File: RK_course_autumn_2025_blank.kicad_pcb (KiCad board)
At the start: 2 copper layers, 65 x 80 mm, 24 parts, among them J1 JST-ZH 6pin, J2 JST-ZH 6pin, J3 Conn_01x02, J4 JST-ZH 6pin, J5 JST-ZH 6pin, J6 Conn_01x03

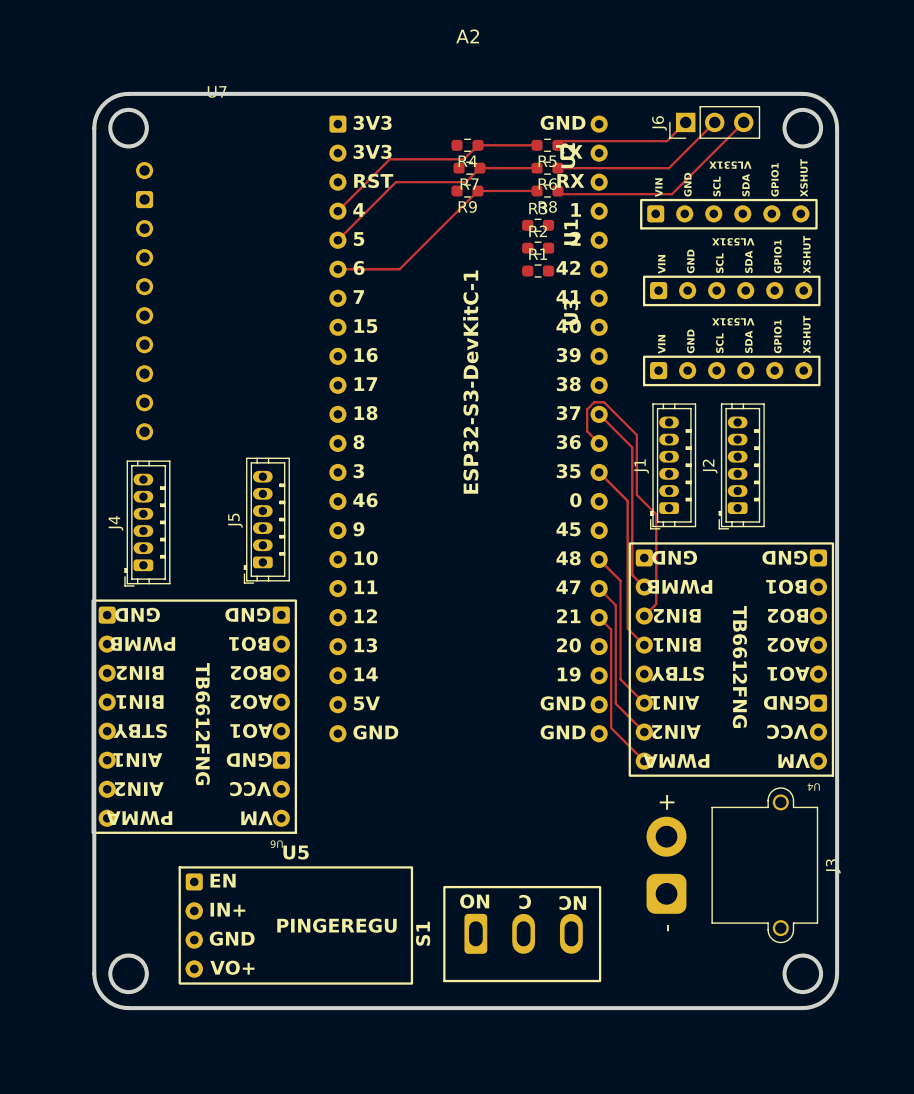
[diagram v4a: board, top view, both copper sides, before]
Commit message: Added traces to PCB to see if possible. Has to be done again.
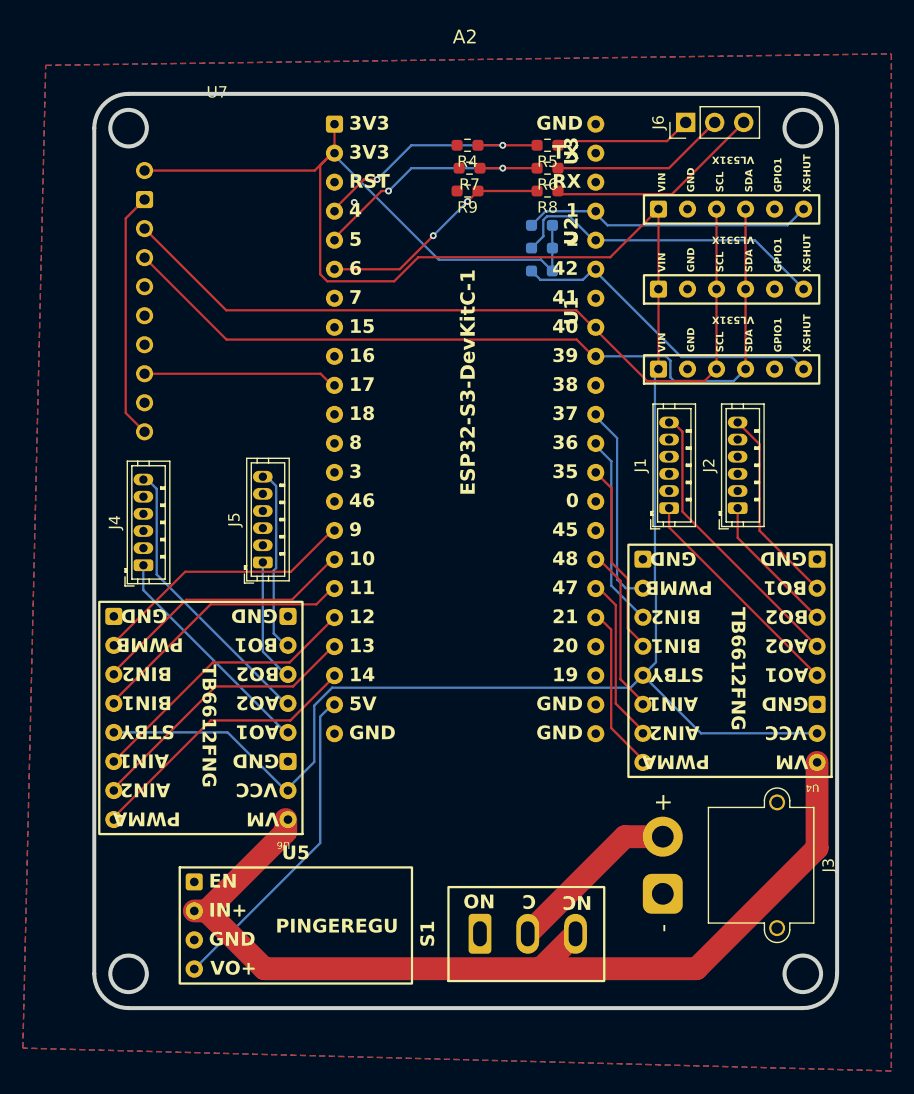
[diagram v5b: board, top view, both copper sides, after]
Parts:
- R1, R2, R3: moved to B.Cu
- moved U3 14.1 mm to (78.0, 70.5)
- moved U1 6.87 mm to (78.0, 84.5)
- moved U2 6.58 mm to (78.0, 77.5)
- moved U6 0.59 mm to (53.2, 129.0)
- moved S1 0.36 mm to (70.0, 139.0)
- moved R1 0.34 mm to (75.4, 81.0), turned to 180 degrees
- moved R2 0.34 mm to (75.4, 79.0), turned to 180 degrees
- moved R3 0.34 mm to (75.4, 77.0), turned to 180 degrees
- moved J3 0.33 mm to (86.0, 135.5)
- moved A2 0.30 mm to (68.7, 68.1)
- moved U4 0.16 mm to (99.5, 124.0)
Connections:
- U7 pad 1: +5V -> +3V3
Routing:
- net +3V3: track 0.00 -> 204.6 mm
- net +12V: track 0.00 -> 83.6 mm
- net SDA: track 0.00 -> 72.4 mm
- net SCL: track 0.00 -> 70.0 mm
- net XSHUT2: track 0.00 -> 28.4 mm
- net +5V: track 0.00 -> 28.1 mm
- net XSHUT1: track 0.00 -> 28.1 mm
- net XSHUT3: track 0.00 -> 25.4 mm
- net Net-(J1-Pin_6): track 0.00 -> 24.8 mm
- net Net-(J4-Pin_6): track 0.00 -> 24.6 mm
- net MOT3DIR2: track 0.00 -> 24.5 mm
- net MOT3DIR1: track 0.00 -> 24.5 mm
- net MOT3SPEED: track 0.00 -> 24.4 mm
- net MOT4SPEED: track 0.00 -> 23.5 mm
- net MOT4DIR1: track 0.00 -> 23.5 mm
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- added copper zone on B.Cu, net GND
- added copper zone on F.Cu, net GND

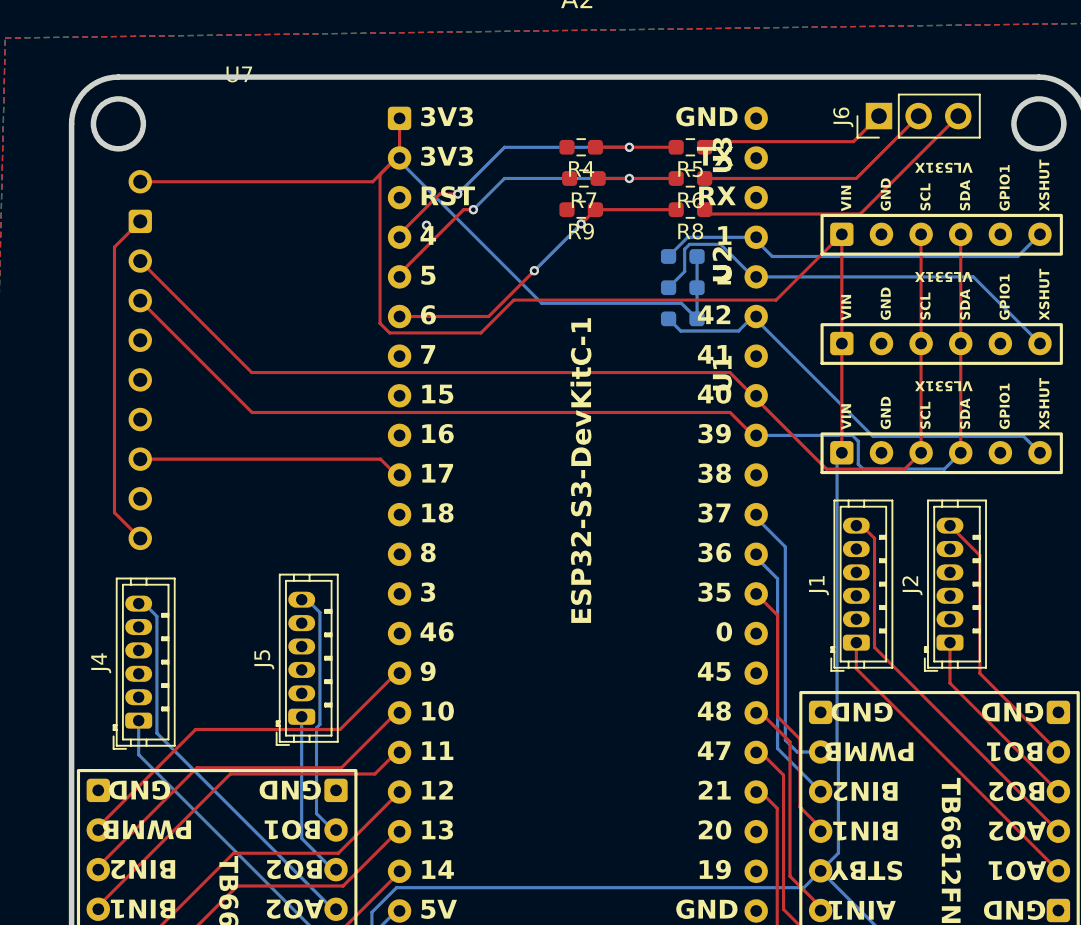
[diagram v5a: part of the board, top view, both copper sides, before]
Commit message: added connector for oled monitor, fixed i2c pins
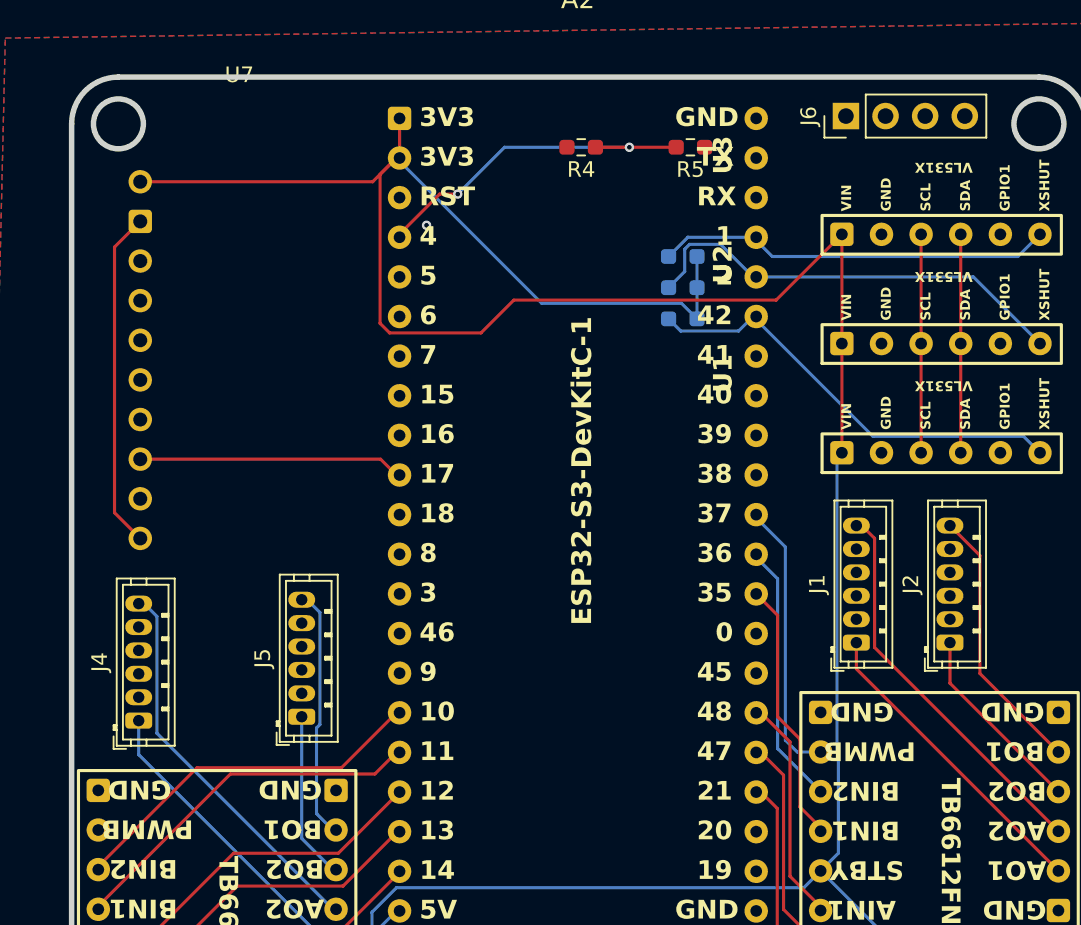
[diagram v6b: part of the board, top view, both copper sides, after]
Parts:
- removed R6, R8: 10k, Resistor_SMD:R_0603_1608Metric_Pad0.98x0.95mm_HandSolder
- removed R7, R9: 5k, Resistor_SMD:R_0603_1608Metric_Pad0.98x0.95mm_HandSolder
- J6: value Conn_01x03 -> Conn_01x04; footprint Connector_PinHeader_2.54mm:PinHeader_1x03_P2.54mm_Vertical -> Connector_PinHeader_2.54mm:PinHeader_1x04_P2.54mm_Vertical
- R5: value 10k -> 15k
- moved J6 2.12 mm to (85.9, 68.0)
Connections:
- A2 pad 11: unconnected-(A2-18-Pad11) -> MOT4SPEED
- A2 pad 12: unconnected-(A2-8-Pad12) -> SDA
- A2 pad 15: MOT4SPEED -> SCL
- A2 pad 30: SCL -> unconnected-(A2-40-Pad30)
- A2 pad 31: SDA -> unconnected-(A2-39-Pad31)
- A2 pad 5: aku2 -> unconnected-(A2-Pad5)
- A2 pad 6: aku3 -> unconnected-(A2-Pad6)
- J6 pad 1: Net-(J6-Pin_1) -> GND
- J6 pad 2: Net-(J6-Pin_2) -> +3V3
- J6 pad 3: Net-(J6-Pin_3) -> SCL
- R5 pad 1: Net-(J6-Pin_1) -> +12V
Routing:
- net SDA: track 72.4 -> 14.0 mm
- net SCL: track 70.0 -> 14.0 mm
- net MOT4SPEED: track 23.5 -> 0.00 mm
- net aku2: track 22.5 -> 0.00 mm, vias 2 -> 0
- net aku3: track 20.3 -> 0.00 mm, vias 2 -> 0
- net Net-(J6-Pin_3): track 18.6 -> 0.00 mm
- net Net-(J6-Pin_2): track 15.4 -> 0.00 mm
- net Net-(J6-Pin_1): track 12.0 -> 0.00 mm

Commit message: new schematic, PCB tracks not final
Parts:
- added JP1: SolderJumper_3_Open, Jumper:SolderJumper-3_P1.3mm_Open_RoundedPad1.0x1.5mm, F.Cu at (47.7, 87.7)
- added JP2: SolderJumper_2_Open, Jumper:SolderJumper-2_P1.3mm_Open_RoundedPad1.0x1.5mm, F.Cu at (68.8, 89.8)
- added JP3: SolderJumper_2_Open, Jumper:SolderJumper-2_P1.3mm_Open_RoundedPad1.0x1.5mm, F.Cu at (68.8, 93.3)
- added JP4: SolderJumper_2_Open, Jumper:SolderJumper-2_P1.3mm_Open_RoundedPad1.0x1.5mm, F.Cu at (68.7, 99.8)
- added JP5: SolderJumper_2_Open, Jumper:SolderJumper-2_P1.3mm_Open_RoundedPad1.0x1.5mm, F.Cu at (68.7, 96.6)
- added R8: 15k, Resistor_SMD:R_0603_1608Metric_Pad0.98x0.95mm_HandSolder, F.Cu at (70.7, 127.6)
- added R9: 4k7, Resistor_SMD:R_0603_1608Metric_Pad0.98x0.95mm_HandSolder, F.Cu at (70.7, 121.6)
- R4: value 5k -> 4k7
- moved J2 4.50 mm to (97.0, 101.8)
- moved U7 0.85 mm to (46.1, 65.9)
- moved J6 0.53 mm to (85.7, 68.5)
- moved J5 0.35 mm to (50.6, 106.5)
- moved J4 0.20 mm to (40.4, 106.8)
- moved A2 0.18 mm to (68.8, 68.0)
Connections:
- A2 pad 10: INT -> MOT3ENC0
- A2 pad 29: unconnected-(A2-41-Pad29) -> MOT2SPEED
- A2 pad 30: unconnected-(A2-40-Pad30) -> MOT2DIR2
- A2 pad 31: unconnected-(A2-39-Pad31) -> Net-(A2-39)
- A2 pad 32: unconnected-(A2-38-Pad32) -> MOT2DIR1
- A2 pad 33: MOT2SPEED -> Net-(A2-37)
- A2 pad 34: MOT2DIR2 -> Net-(A2-36)
- A2 pad 35: MOT2DIR1 -> Net-(JP5-A)
- A2 pad 5: unconnected-(A2-Pad5) -> INT
- A2 pad 7: unconnected-(A2-Pad7) -> MOT4ENC1
- A2 pad 8: unconnected-(A2-15-Pad8) -> MOT4ENC0
- A2 pad 9: unconnected-(A2-16-Pad9) -> MOT3ENC1
- J1 pad 2: unconnected-(J1-Pin_2-Pad2) -> GND
- J1 pad 3: unconnected-(J1-Pin_3-Pad3) -> MOT1ENC0
- J1 pad 4: unconnected-(J1-Pin_4-Pad4) -> MOT1ENC1
- J1 pad 5: unconnected-(J1-Pin_5-Pad5) -> +3V3
- J2 pad 2: unconnected-(J2-Pin_2-Pad2) -> GND
- J2 pad 3: unconnected-(J2-Pin_3-Pad3) -> MOT2ENC0
- J2 pad 4: unconnected-(J2-Pin_4-Pad4) -> MOT2ENC1
- J2 pad 5: unconnected-(J2-Pin_5-Pad5) -> +3V3
- J4 pad 2: unconnected-(J4-Pin_2-Pad2) -> GND
- J4 pad 3: unconnected-(J4-Pin_3-Pad3) -> MOT3ENC0
- J4 pad 4: unconnected-(J4-Pin_4-Pad4) -> MOT3ENC1
- J4 pad 5: unconnected-(J4-Pin_5-Pad5) -> +3V3
- J5 pad 2: unconnected-(J5-Pin_2-Pad2) -> GND
- J5 pad 3: unconnected-(J5-Pin_3-Pad3) -> MOT4ENC0
- J5 pad 4: unconnected-(J5-Pin_4-Pad4) -> MOT4ENC1
- J5 pad 5: unconnected-(J5-Pin_5-Pad5) -> +3V3
- U4 pad 12: +3V3 -> STBY
- U6 pad 12: +3V3 -> STBY
- U7 pad 7: unconnected-(U7-ADO-Pad7) -> Net-(JP1-C)
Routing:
- net +12V: track 83.6 -> 212.9 mm
- net SDA: track 14.0 -> 103.7 mm
- net SCL: track 14.0 -> 99.7 mm, vias 0 -> 2
- net +3V3: track 204.6 -> 285.1 mm, vias 0 -> 1
- net STBY: track 0.00 -> 61.3 mm
- net MOT2ENC0: track 0.00 -> 37.1 mm
- net MOT2ENC1: track 0.00 -> 34.2 mm
- net MOT4SPEED: track 0.00 -> 32.2 mm, vias 0 -> 3
- net MOT4DIR1: track 23.5 -> 50.5 mm
- net MOT4ENC1: track 0.00 -> 23.7 mm, vias 0 -> 1
- net MOT4DIR2: track 23.5 -> 46.4 mm
- net MOT3ENC1: track 0.00 -> 22.8 mm, vias 0 -> 1
- net MOT3ENC0: track 0.00 -> 22.3 mm, vias 0 -> 1
- net MOT4ENC0: track 0.00 -> 22.3 mm, vias 0 -> 1
- net Net-(A2-36): track 0.00 -> 21.8 mm, vias 0 -> 1
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
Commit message: now with tracks
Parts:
- added R6: 15k, Resistor_SMD:R_0603_1608Metric_Pad0.98x0.95mm_HandSolder, B.Cu at (47.8, 128.7)
- added R7: 4k7, Resistor_SMD:R_0603_1608Metric_Pad0.98x0.95mm_HandSolder, B.Cu at (46.9, 125.4)
- JP1, JP2, JP3, JP4, JP5, R4, R5, R8, R9: moved to B.Cu
- moved R8 22.3 mm to (91.4, 119.3)
- moved R9 21.7 mm to (91.3, 114.8)
- moved U5 19.7 mm to (63.0, 142.4), turned to 180 degrees
- moved JP5 5.84 mm to (73.3, 100.1), turned to 180 degrees
- moved JP4 5.43 mm to (73.3, 97.0), turned to 180 degrees
- moved JP2 4.60 mm to (73.4, 89.9), turned to 180 degrees
- moved JP3 4.60 mm to (73.4, 93.4), turned to 180 degrees
- moved JP1 4.22 mm to (43.4, 87.6)
- moved R3 1.44 mm to (75.1, 75.6), turned to 0 degrees
- moved R5 0.88 mm to (75.0, 69.9)
- moved R2 0.87 mm to (75.1, 78.2), turned to 0 degrees
- moved U7 0.65 mm to (45.5, 65.9)
- moved R4 0.61 mm to (68.3, 69.9)
- moved R1 0.45 mm to (75.1, 80.7), turned to 0 degrees
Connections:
- A2 pad 10: MOT3ENC0 -> MOT4ENC0
- A2 pad 7: MOT4ENC1 -> MOT3ENC1
- A2 pad 8: MOT4ENC0 -> MOT3ENC0
- A2 pad 9: MOT3ENC1 -> MOT4ENC1
- JP4 pad 2: MOT1ENC0 -> MOT1ENC1
- JP5 pad 2: MOT1ENC1 -> MOT1ENC0
- R8 pad 2: STBY -> STBY1
- R9 pad 1: STBY -> STBY1
- U4 pad 12: STBY -> STBY1
- U6 pad 12: STBY -> STBY2
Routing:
- net +3V3: track 285.1 -> 222.3 mm, vias 1 -> 2
- net STBY: track 61.3 -> 0.00 mm
- net +12V: track 212.9 -> 159.3 mm, vias 0 -> 1
- net MOT4DIR1: track 50.5 -> 23.5 mm, vias 0 -> 2
- net MOT4DIR2: track 46.4 -> 23.5 mm, vias 0 -> 2
- net Net-(A2-36): track 21.8 -> 6.71 mm, vias 1 -> 0
- net MOT3DIR2: track 40.4 -> 26.2 mm
- net STBY2: track 0.00 -> 13.4 mm, vias 0 -> 1
- net +5V: track 29.5 -> 18.4 mm
- net STBY1: track 0.00 -> 10.00 mm
- net Net-(JP5-A): track 16.8 -> 6.95 mm, vias 1 -> 0
- net Net-(A2-37): track 15.3 -> 6.21 mm, vias 1 -> 0
- net Net-(A2-39): track 15.9 -> 6.85 mm, vias 1 -> 0
- net MOT4ENC1: track 23.7 -> 16.2 mm
- net MOT4ENC0: track 22.3 -> 16.1 mm
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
